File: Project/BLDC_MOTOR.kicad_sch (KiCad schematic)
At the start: 27 parts, among them Q201 2N7002

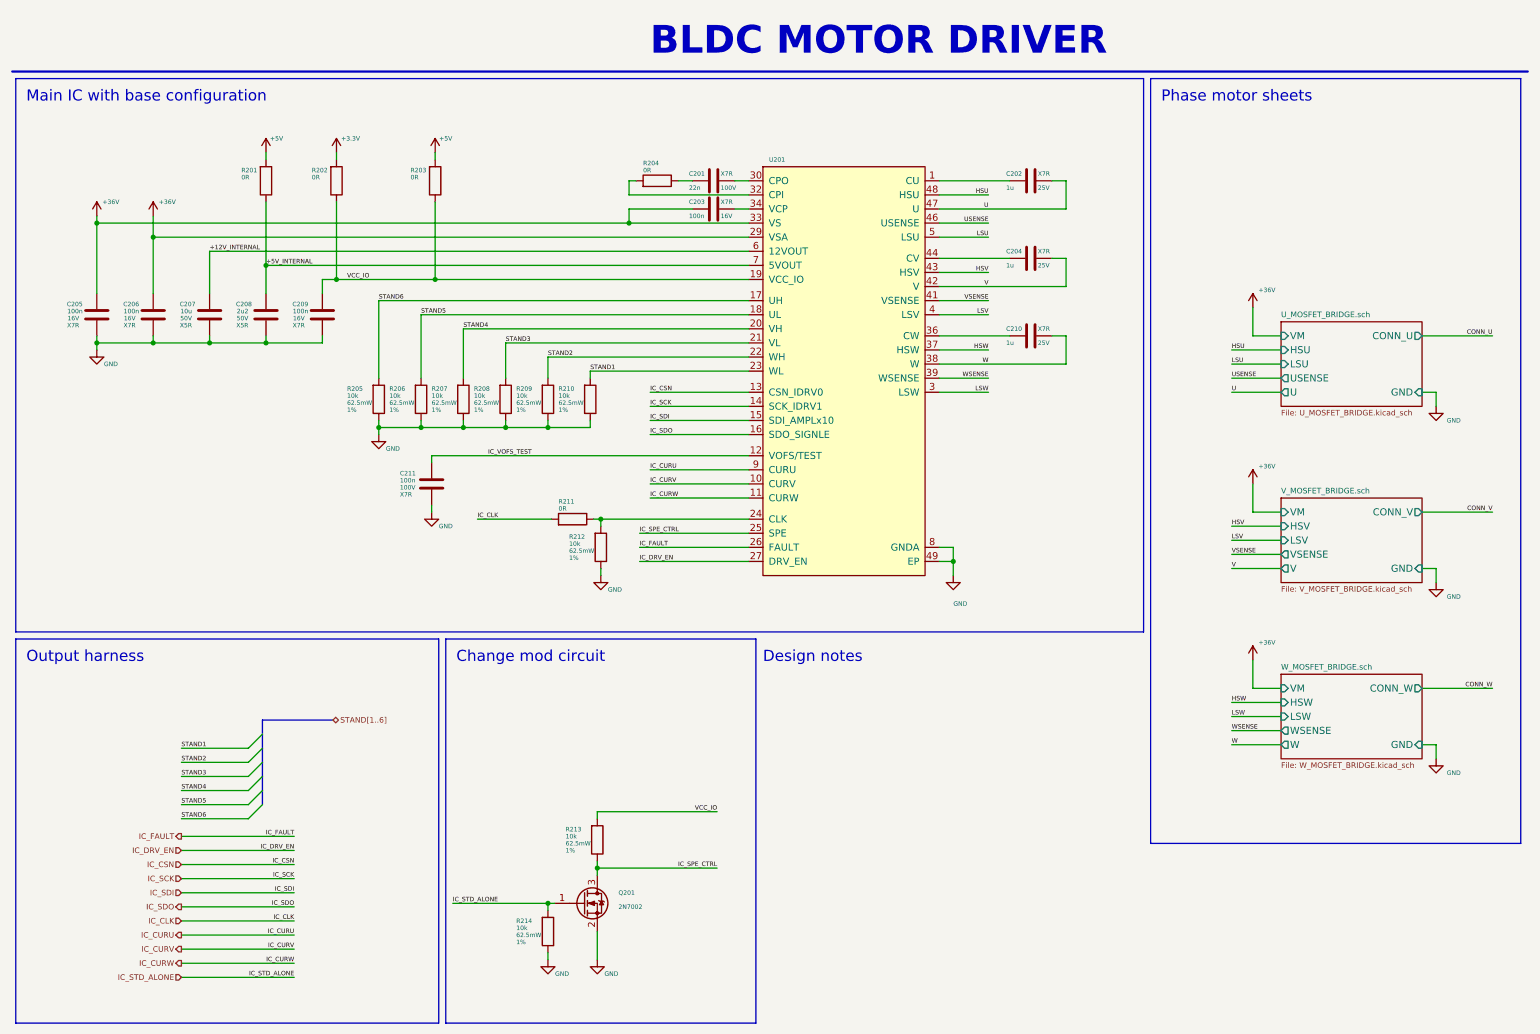
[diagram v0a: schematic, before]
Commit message: Cleaning files, added testpoints
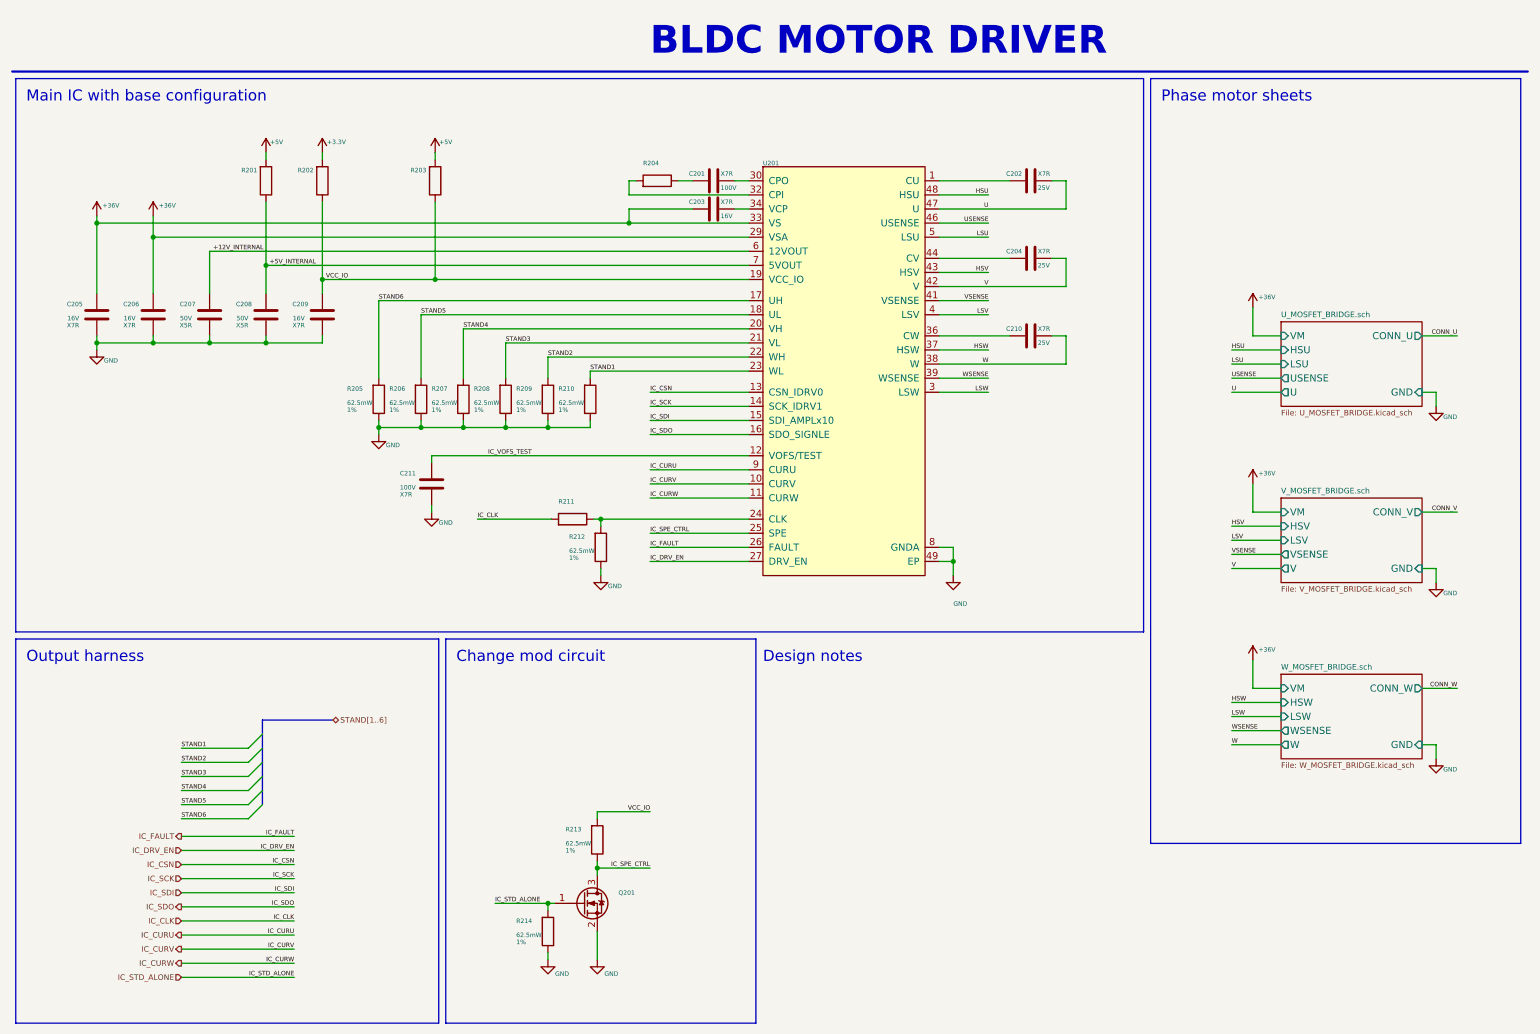
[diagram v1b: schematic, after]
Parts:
- C201: value 22n -> (none); footprint Capacitor_SMD:C_0603_1608Metric -> (none)
- C202, C204, C210: value 1u -> (none); footprint Capacitor_SMD:C_0603_1608Metric -> (none)
- C203, C205, C206, C209, C211: value 100n -> (none); footprint Capacitor_SMD:C_0603_1608Metric -> (none)
- C207: value 10u -> (none); footprint Capacitor_SMD:C_1206_3216Metric -> (none)
- C208: value 2u2 -> (none); footprint Capacitor_SMD:C_0603_1608Metric -> (none)
- Q201: value 2N7002 -> (none); footprint Package_TO_SOT_SMD:SOT-23 -> (none)
- R201, R202, R203, R211: value 0R -> (none); footprint Resistor_SMD:R_0402_1005Metric -> (none)
- R204: value 0R -> (none); footprint Resistor_SMD:R_0603_1608Metric -> (none)
- R205, R206, R207, R208, R209, R210, R212, R213, R214: value 10k -> (none); footprint Resistor_SMD:R_0402_1005Metric -> (none)
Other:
- moved on the sheet: R202
